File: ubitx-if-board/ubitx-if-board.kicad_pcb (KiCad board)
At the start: 2 copper layers, 32.3 x 32.7 mm, 42 parts, among them J1 Signal, J2 Power, J3 RX IN, J4 RX OUT, J5 TX IN, J6 TX OUT, Q101 BFR92, Q102 BFR92, Q103 BFR92, Q201 BFR92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

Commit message: * Layout updates * Fix text labelling * Add my text bits here!
This was sent to oshpark as 1.0 today for printing!
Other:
- board text added: "A"
- board text added: "B"
- board text added: "GND"
- board text added: "RXB"
- board text added: "RXIN"
- board text added: "RXOUT"
- board text added: "TXB"
- board text added: "TXIN"
- board text added: "TXOUT"
- board text added: "uBITX IF amplifier pair Adrian Chadd <adrian@freebsd.org> v1.0 14/Mar/2021"

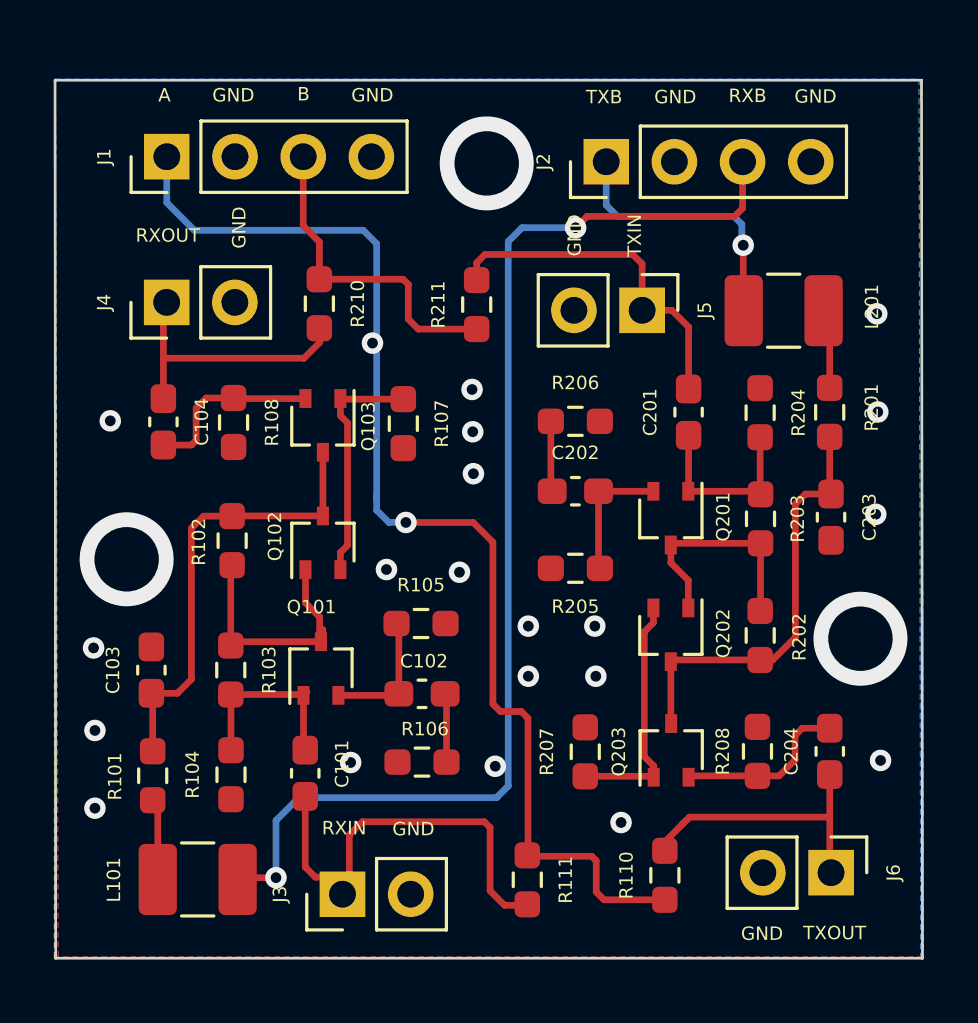
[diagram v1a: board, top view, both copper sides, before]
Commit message: WHOOPS - my last minute vias were err, wrong.
THIS is now what's sent as v1.0 to print at oshpark!
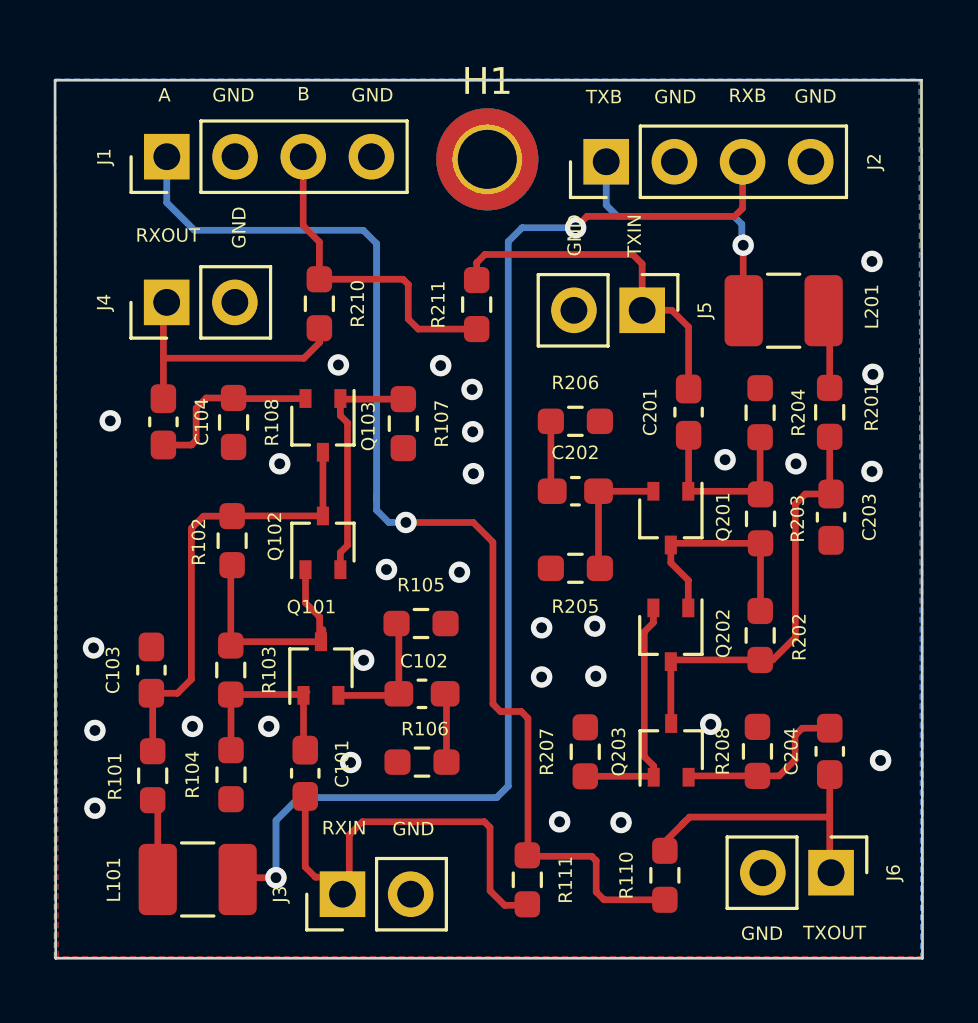
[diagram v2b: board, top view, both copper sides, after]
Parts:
- added H1: MountingHole_Pad, MountingHole:MountingHole_2.2mm_M2_DIN965_Pad_TopBottom, F.Cu at (28.0, 15.0)
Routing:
- net GND: vias 24 -> 29
